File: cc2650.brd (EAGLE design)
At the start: 50.8 x 22.9 mm, 23 parts, among them IC1 TPS73133DBVR, IC4 CC2650MODAMOHR, SW1 SPST_TACT-KMR2, SW3 SPST_TACT-KMR2

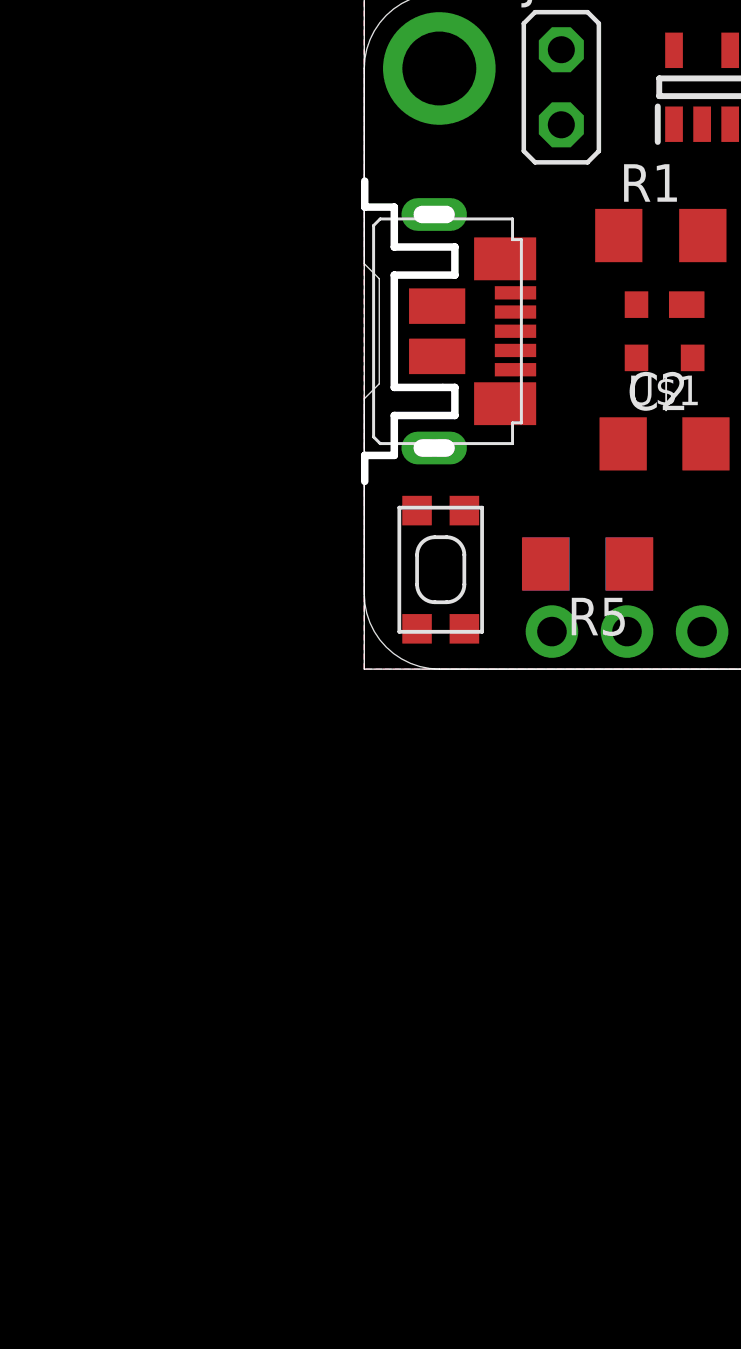
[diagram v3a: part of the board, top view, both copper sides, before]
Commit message: changed usb to AMP lab part.
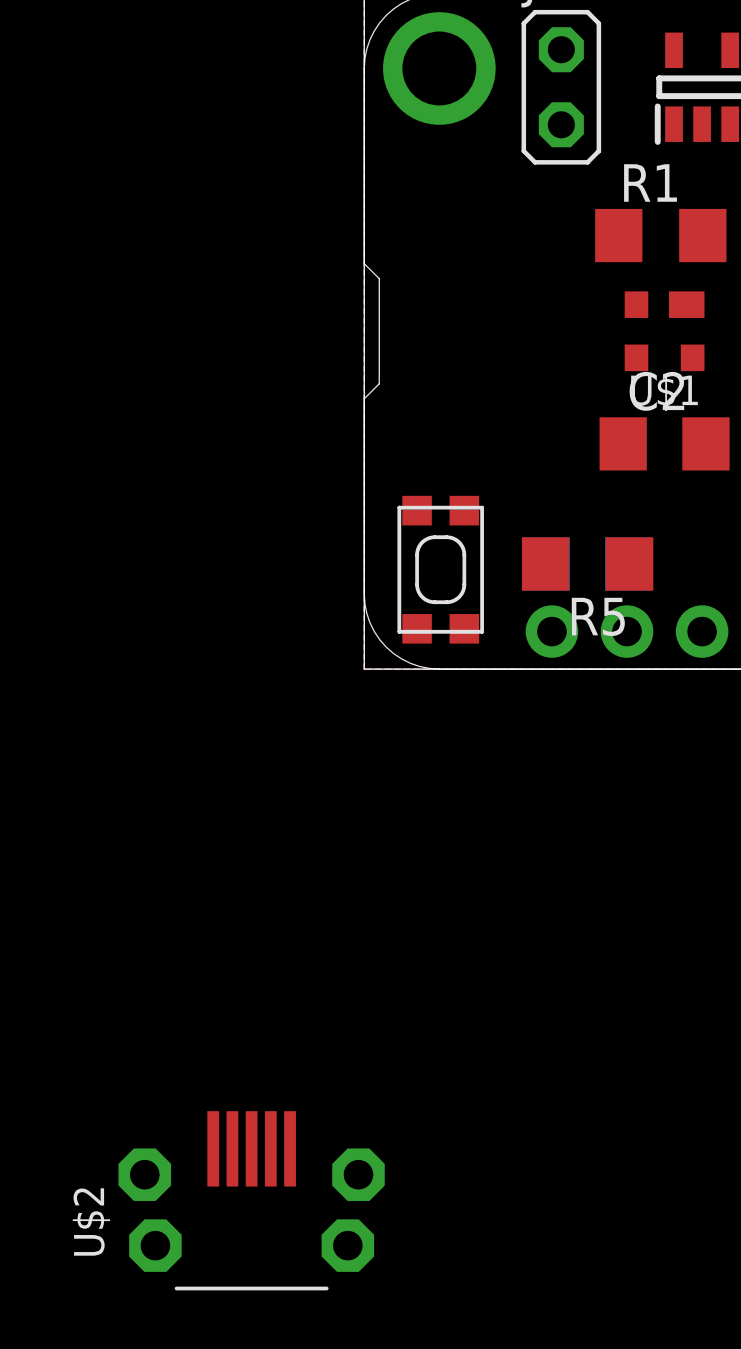
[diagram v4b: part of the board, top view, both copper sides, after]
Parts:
- removed USB101: (no value), MSP_Connectors:MOLEX_105164-0001
- added U$2: 2040002, AMP_Ruler-LT1370:2040002
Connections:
- net D+: no longer USB101.D+
- net D-: no longer USB101.D-
- net GND: no longer USB101.GND
- net VBUS: no longer USB101.VBUS
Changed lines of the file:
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@@
 <attribute name="OC_NEWARK" value="58M7854" x="2.5865" y="3.3625" size="1.778" layer="27" rot="R90" display="off"/>
-</element>
-<element name="USB101" library="MSP_Connectors" package="MOLEX_105164-0001" value="" x="1.016" y="11.43" rot="R90">
-<attribute name="MF" value="" x="1.016" y="11.43" size="1.778" layer="27" rot="R90" display="off"/>
-<attribute name="MPN" value="105164-0001" x="1.016" y="11.43" size="1.778" layer="27" rot="R90" display="off"/>
-<attribute name="OC_NEWARK" value="99Y3224" x="1.016" y="11.43" size="1.778" layer="27" rot="R90" display="off"/>
 </element>
 <element name="IC1" library="TPS73133DBVR" package="SOT95P280X145-5N" value="TPS73133DBVR" x="11.43" y="19.685" smashed="yes" rot="R90">
@@
 <attribute name="OC_NEWARK" value="48C2970" x="10.16" y="7.62" size="1.778" layer="27" display="off"/>
 </element>
+<element name="U$2" library="AMP_Ruler-LT1370" package="2040002" value="2040002" x="-3.81" y="-20.955"/>
 </elements>
 <signals>
@@
 <vertex x="0" y="0"/>
 </polygon>
-<contactref element="USB101" pad="GND"/>
 <contactref element="IC1" pad="4"/>
 <contactref element="SW3" pad="1"/>
@@
 <wire x1="18.415" y1="10.315" x2="23.495" y2="13.9035" width="0" layer="19" extent="1-1"/>
 <wire x1="15.8115" y1="10.315" x2="18.415" y2="10.315" width="0" layer="19" extent="1-1"/>
-<wire x1="10.91" y1="12.33" x2="15.8115" y2="10.315" width="0" layer="19" extent="1-1"/>
-<wire x1="5.116" y1="12.73" x2="10.91" y2="12.33" width="0" layer="19" extent="1-1"/>
+<wire x1="11.56" y1="7.62" x2="15.8115" y2="10.315" width="0" layer="19" extent="1-1"/>
+<wire x1="10.91" y1="12.33" x2="11.56" y2="7.62" width="0" layer="19" extent="1-1"/>
+<wire x1="8.9565" y1="3.556" x2="11.56" y2="7.62" width="0" layer="19" extent="1-16"/>
+<wire x1="13.97" y1="1.27" x2="8.9565" y2="3.556" width="0" layer="19" extent="16-16"/>
 <wire x1="11.43" y1="18.435" x2="10.91" y2="12.33" width="0" layer="19" extent="1-1"/>
 <wire x1="12.38" y1="20.935" x2="11.43" y2="18.435" width="0" layer="19" extent="1-1"/>
-<wire x1="1.7865" y1="5.3625" x2="5.116" y2="12.73" width="0" layer="19" extent="1-1"/>
+<wire x1="1.7865" y1="5.3625" x2="8.9565" y2="3.556" width="0" layer="19" extent="1-16"/>
 <wire x1="1.7865" y1="1.3625" x2="1.7865" y2="5.3625" width="0" layer="19" extent="1-1"/>
-<wire x1="8.9565" y1="3.556" x2="1.7865" y2="5.3625" width="0" layer="19" extent="1-16"/>
-<wire x1="13.97" y1="1.27" x2="8.9565" y2="3.556" width="0" layer="19" extent="16-16"/>
-<wire x1="11.56" y1="7.62" x2="1.7865" y2="1.3625" width="0" layer="19" extent="1-1"/>
 </signal>
 <signal name="NRESET">
@@
 </signal>
 <signal name="VBUS" class="2">
-<contactref element="USB101" pad="VBUS"/>
 <contactref element="MS1" pad="26"/>
 <contactref element="U$1" pad="4"/>
@@
 <wire x1="8.611" y1="14.6685" x2="10.48" y2="18.435" width="0" layer="19" extent="1-1"/>
 <wire x1="11.11" y1="10.53" x2="8.611" y2="14.6685" width="0" layer="19" extent="1-1"/>
-<wire x1="5.116" y1="10.13" x2="8.611" y2="14.6685" width="0" layer="19" extent="1-1"/>
-<wire x1="8.76" y1="7.62" x2="5.116" y2="10.13" width="0" layer="19" extent="1-1"/>
+<wire x1="8.76" y1="7.62" x2="11.11" y2="10.53" width="0" layer="19" extent="1-1"/>
 </signal>
 <signal name="EN">
@@
 </signal>
 <signal name="D-">
-<contactref element="USB101" pad="D-"/>
 <contactref element="U$1" pad="3"/>
-<wire x1="9.21" y1="10.53" x2="5.116" y2="10.78" width="0" layer="19" extent="1-1"/>
 </signal>
 <signal name="D+">
-<contactref element="USB101" pad="D+"/>
 <contactref element="U$1" pad="2"/>
-<wire x1="9.21" y1="12.33" x2="5.116" y2="11.43" width="0" layer="19" extent="1-1"/>
 </signal>
 </signals>

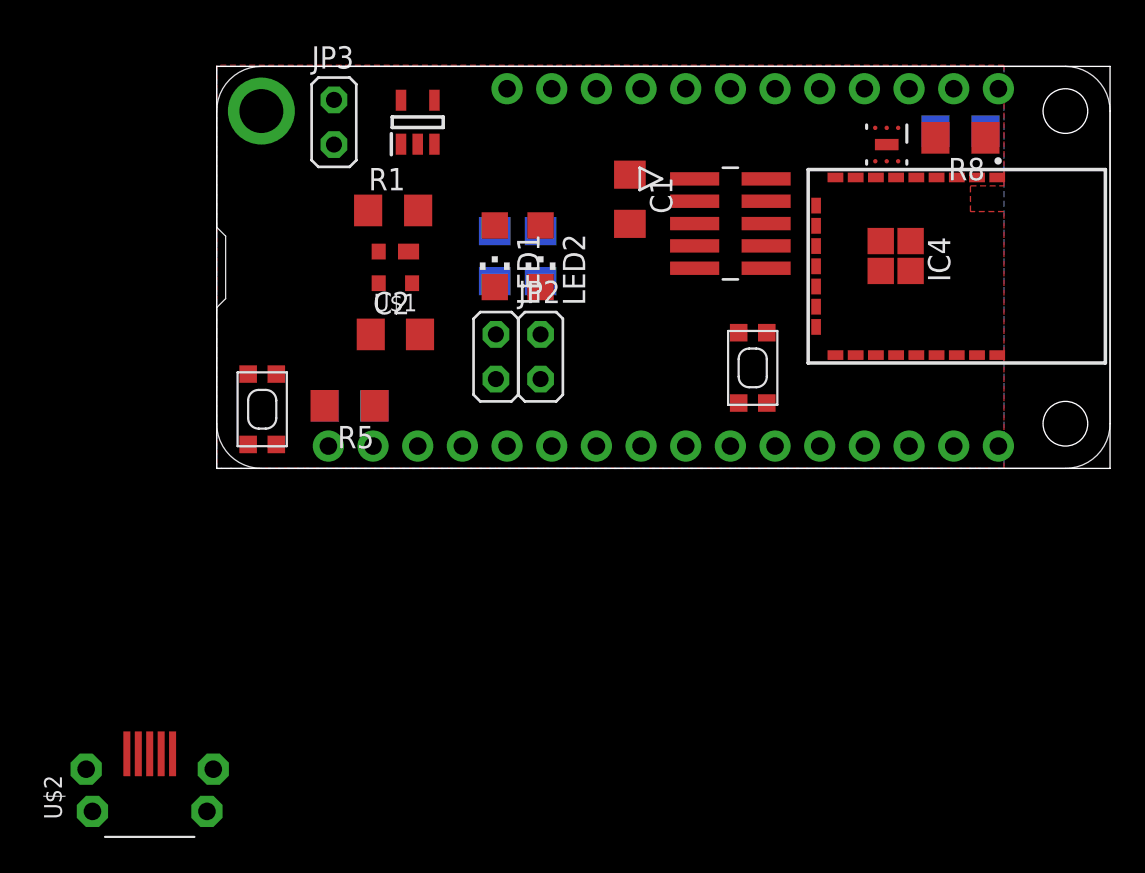
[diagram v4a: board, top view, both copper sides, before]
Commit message: changed USB circuit to closer match layout of AMP card.
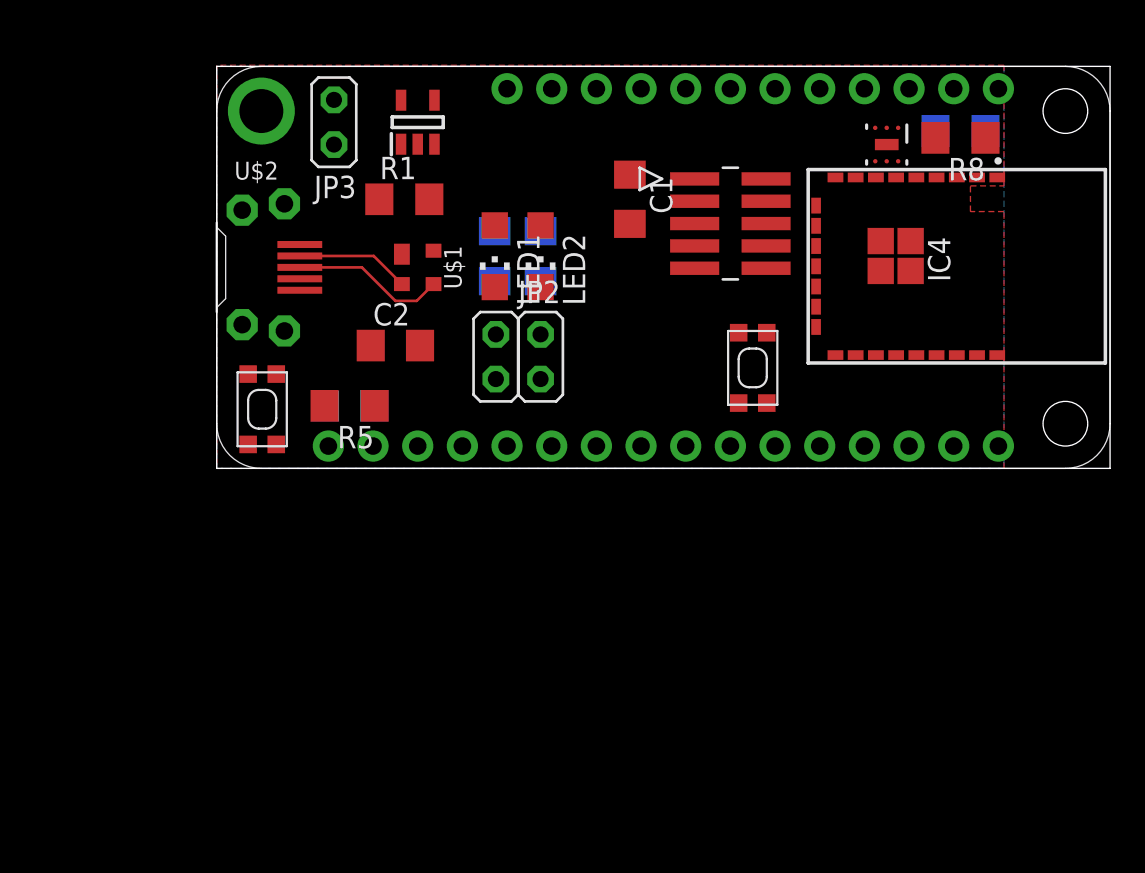
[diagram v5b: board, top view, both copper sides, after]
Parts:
- moved U$2 32.6 mm to (0.00, 11.4), turned to 270 degrees
- moved U$1 1.27 mm to (11.4, 11.4), turned to 270 degrees
- moved R1 0.90 mm to (10.7, 15.3)
- moved C2 0.63 mm to (10.2, 6.99)
- turned JP3 to 180 degrees
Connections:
- net D+: now also U$1.3, U$2.3; no longer U$1.2
- net D-: now also U$1.2, U$2.2; no longer U$1.3
- net GND: now also U$2.5
- net VBUS: now also U$2.1
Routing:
- net D+: track 0.00 -> 8.79 mm
- net D-: track 0.00 -> 6.47 mm
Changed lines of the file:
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@@
 <wire x1="50.8" y1="22.86" x2="0" y2="22.86" width="0" layer="20"/>
 <wire x1="0" y1="22.86" x2="0" y2="0" width="0" layer="20"/>
-<dimension x1="0" y1="0" x2="0" y2="22.86" x3="-1.905" y3="11.43" textsize="1.778" layer="47" unit="inch"/>
+<dimension x1="0" y1="0" x2="0" y2="22.86" x3="-5.715" y3="11.43" textsize="1.778" layer="47" unit="inch"/>
 <dimension x1="0" y1="0" x2="50.8" y2="0" x3="25.4" y3="-3.81" textsize="1.778" layer="47" unit="inch"/>
 <dimension x1="0" y1="22.9235" x2="10.795" y2="22.86" x3="5.408440625" y3="24.7518625" textsize="1.778" layer="47" unit="inch"/>
 <dimension x1="0" y1="22.9235" x2="16.51" y2="22.86" x3="8.27451875" y3="27.966790625" textsize="1.778" layer="47" unit="inch"/>
+<dimension x1="0" y1="0" x2="0" y2="11.43" x3="-2.54" y3="5.715" textsize="1.778" layer="47" unit="inch"/>
 </plain>
 <attributes>
@@
 <attribute name="VALUE" x="14.605" y="2.032" size="1.27" layer="27" ratio="10"/>
 </element>
-<element name="R1" library="adafruit" package="R1206" value="100k" x="10.033" y="14.6685">
-<attribute name="MF" value="" x="10.033" y="14.6685" size="1.778" layer="27" display="off"/>
-<attribute name="MPN" value="CR1206-FX-4700ELF" x="10.033" y="14.6685" size="1.778" layer="27" display="off"/>
-<attribute name="OC_NEWARK" value="06X5194" x="10.033" y="14.6685" size="1.778" layer="27" display="off"/>
+<element name="R1" library="adafruit" package="R1206" value="100k" x="10.668" y="15.3035">
+<attribute name="MF" value="" x="10.668" y="15.3035" size="1.778" layer="27" display="off"/>
+<attribute name="MPN" value="CR1206-FX-4700ELF" x="10.668" y="15.3035" size="1.778" layer="27" display="off"/>
+<attribute name="OC_NEWARK" value="06X5194" x="10.668" y="15.3035" size="1.778" layer="27" display="off"/>
 </element>
 <element name="MS1" library="wing_modified" package="FEATHERWING_DIM" value="FEATHERWING_NODIM" x="0" y="0"/>
@@
 <attribute name="OC_NEWARK" value="08N6744" x="-3.175" y="18.415" size="1.778" layer="27" display="off"/>
 </element>
-<element name="JP3" library="jumper" package="JP1M" value="PWR_LED" x="6.6675" y="19.685">
-<attribute name="MF" value="" x="6.6675" y="19.685" size="1.778" layer="27" display="off"/>
-<attribute name="MPN" value="2211S-02G" x="6.6675" y="19.685" size="1.778" layer="27" display="off"/>
-<attribute name="OC_NEWARK" value="08N6744" x="6.6675" y="19.685" size="1.778" layer="27" display="off"/>
-</element>
-<element name="U$1" library="AMP_Ruler-LT1370" package="SOT-143" value="TPD2E001" x="10.16" y="11.43" rot="R180"/>
-<element name="C2" library="adafruit" package="C1206" value="0.1u" x="10.16" y="7.62">
-<attribute name="MF" value="VISHAY/VITRAMON" x="10.16" y="7.62" size="1.778" layer="27" display="off"/>
-<attribute name="MPN" value="VJ1206Y102KXBAC" x="10.16" y="7.62" size="1.778" layer="27" display="off"/>
-<attribute name="OC_NEWARK" value="48C2970" x="10.16" y="7.62" size="1.778" layer="27" display="off"/>
-</element>
-<element name="U$2" library="AMP_Ruler-LT1370" package="2040002" value="2040002" x="-3.81" y="-20.955"/>
+<element name="JP3" library="jumper" package="JP1M" value="PWR_LED" x="6.6675" y="19.685" rot="R180">
+<attribute name="MF" value="" x="6.6675" y="19.685" size="1.778" layer="27" rot="R180" display="off"/>
+<attribute name="MPN" value="2211S-02G" x="6.6675" y="19.685" size="1.778" layer="27" rot="R180" display="off"/>
+<attribute name="OC_NEWARK" value="08N6744" x="6.6675" y="19.685" size="1.778" layer="27" rot="R180" display="off"/>
+</element>
+<element name="U$1" library="AMP_Ruler-LT1370" package="SOT-143" value="TPD2E001" x="11.43" y="11.43" rot="R270"/>
+<element name="C2" library="adafruit" package="C1206" value="0.1u" x="10.16" y="6.985">
+<attribute name="MF" value="VISHAY/VITRAMON" x="10.16" y="6.985" size="1.778" layer="27" display="off"/>
+<attribute name="MPN" value="VJ1206Y102KXBAC" x="10.16" y="6.985" size="1.778" layer="27" display="off"/>
+<attribute name="OC_NEWARK" value="48C2970" x="10.16" y="6.985" size="1.778" layer="27" display="off"/>
+</element>
+<element name="U$2" library="AMP_Ruler-LT1370" package="2040002" value="2040002" x="0" y="11.43" rot="R270"/>
 </elements>
 <signals>
@@
 <contactref element="U$1" pad="1"/>
 <contactref element="C2" pad="2"/>
+<contactref element="U$2" pad="5"/>
 <wire x1="42.084" y1="16.5435" x2="44.384" y2="16.5435" width="0" layer="19" extent="1-1"/>
 <wire x1="38.1" y1="18.415" x2="42.084" y2="16.5435" width="0" layer="19" extent="1-1"/>
@@
 <wire x1="18.415" y1="10.315" x2="23.495" y2="13.9035" width="0" layer="19" extent="1-1"/>
 <wire x1="15.8115" y1="10.315" x2="18.415" y2="10.315" width="0" layer="19" extent="1-1"/>
-<wire x1="11.56" y1="7.62" x2="15.8115" y2="10.315" width="0" layer="19" extent="1-1"/>
-<wire x1="10.91" y1="12.33" x2="11.56" y2="7.62" width="0" layer="19" extent="1-1"/>
-<wire x1="8.9565" y1="3.556" x2="11.56" y2="7.62" width="0" layer="19" extent="1-16"/>
+<wire x1="11.56" y1="6.985" x2="15.8115" y2="10.315" width="0" layer="19" extent="1-1"/>
+<wire x1="10.53" y1="12.18" x2="11.56" y2="6.985" width="0" layer="19" extent="1-1"/>
+<wire x1="8.9565" y1="3.556" x2="11.56" y2="6.985" width="0" layer="19" extent="1-16"/>
 <wire x1="13.97" y1="1.27" x2="8.9565" y2="3.556" width="0" layer="19" extent="16-16"/>
-<wire x1="11.43" y1="18.435" x2="10.91" y2="12.33" width="0" layer="19" extent="1-1"/>
+<wire x1="11.43" y1="18.435" x2="10.53" y2="12.18" width="0" layer="19" extent="1-1"/>
 <wire x1="12.38" y1="20.935" x2="11.43" y2="18.435" width="0" layer="19" extent="1-1"/>
-<wire x1="1.7865" y1="5.3625" x2="8.9565" y2="3.556" width="0" layer="19" extent="1-16"/>
+<wire x1="4.725" y1="10.13" x2="10.53" y2="12.18" width="0" layer="19" extent="1-1"/>
+<wire x1="1.7865" y1="5.3625" x2="4.725" y2="10.13" width="0" layer="19" extent="1-1"/>
 <wire x1="1.7865" y1="1.3625" x2="1.7865" y2="5.3625" width="0" layer="19" extent="1-1"/>
 </signal>
@@
 <wire x1="8.9785" y1="3.556" x2="15.875" y2="5.08" width="0" layer="19" extent="1-1"/>
 <wire x1="8.89" y1="1.27" x2="8.9785" y2="3.556" width="0" layer="19" extent="1-1"/>
-<wire x1="6.6675" y1="20.955" x2="8.89" y2="1.27" width="0" layer="19" extent="1-1"/>
+<wire x1="6.6675" y1="18.415" x2="8.89" y2="1.27" width="0" layer="19" extent="1-1"/>
 </signal>
 <signal name="VBAT">
@@
 <contactref element="R1" pad="1"/>
 <contactref element="C2" pad="1"/>
+<contactref element="U$2" pad="1"/>
 <wire x1="10.48" y1="18.435" x2="21.59" y2="21.59" width="0" layer="19" extent="1-1"/>
-<wire x1="8.611" y1="14.6685" x2="10.48" y2="18.435" width="0" layer="19" extent="1-1"/>
-<wire x1="11.11" y1="10.53" x2="8.611" y2="14.6685" width="0" layer="19" extent="1-1"/>
-<wire x1="8.76" y1="7.62" x2="11.11" y2="10.53" width="0" layer="19" extent="1-1"/>
+<wire x1="9.246" y1="15.3035" x2="10.48" y2="18.435" width="0" layer="19" extent="1-1"/>
+<wire x1="12.33" y1="12.38" x2="9.246" y2="15.3035" width="0" layer="19" extent="1-1"/>
+<wire x1="4.725" y1="12.73" x2="9.246" y2="15.3035" width="0" layer="19" extent="1-1"/>
+<wire x1="8.76" y1="6.985" x2="12.33" y2="12.38" width="0" layer="19" extent="1-1"/>
 </signal>
 <signal name="EN">
@@
 <contactref element="MS1" pad="27"/>
 <wire x1="12.38" y1="18.435" x2="19.05" y2="21.59" width="0" layer="19" extent="1-1"/>
-<wire x1="11.455" y1="14.6685" x2="12.38" y2="18.435" width="0" layer="19" extent="1-1"/>
+<wire x1="12.09" y1="15.3035" x2="12.38" y2="18.435" width="0" layer="19" extent="1-1"/>
 </signal>
 <signal name="N$1">
@@
 <contactref element="IC1" pad="5"/>
 <contactref element="JP3" pad="1"/>
-<wire x1="10.48" y1="20.935" x2="6.6675" y2="18.415" width="0" layer="19" extent="1-1"/>
+<wire x1="10.48" y1="20.935" x2="6.6675" y2="20.955" width="0" layer="19" extent="1-1"/>
 </signal>
 <signal name="D-">
+<contactref element="U$2" pad="2"/>
+<contactref element="U$1" pad="2"/>
+<wire x1="4.725" y1="12.08" x2="8.93" y2="12.08" width="0.1524" layer="1"/>
+<wire x1="8.93" y1="12.08" x2="10.53" y2="10.48" width="0.1524" layer="1"/>
+</signal>
+<signal name="D+">
+<contactref element="U$2" pad="3"/>
 <contactref element="U$1" pad="3"/>
-</signal>
-<signal name="D+">
-<contactref element="U$1" pad="2"/>
+<wire x1="4.725" y1="11.43" x2="8.255" y2="11.43" width="0.1524" layer="1"/>
+<wire x1="8.255" y1="11.43" x2="10.16" y2="9.525" width="0.1524" layer="1"/>
+<wire x1="10.16" y1="9.525" x2="11.375" y2="9.525" width="0.1524" layer="1"/>
+<wire x1="11.375" y1="9.525" x2="12.33" y2="10.48" width="0.1524" layer="1"/>
 </signal>
 </signals>
